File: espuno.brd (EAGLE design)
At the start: 68.6 x 53.3 mm, 62 parts, among them J1 ARDUINO_R3_SHIELD, T1 FDN340P, U1 ADS1115IDGST, U2 NCP1117ST50T3G, U3 LP2985-33DBVR, U4 FT232R, U5 LMV358IDGKR, U6 MCP73831, U7 TPS61200, X1 POWERSUPPLY_DC21MMX

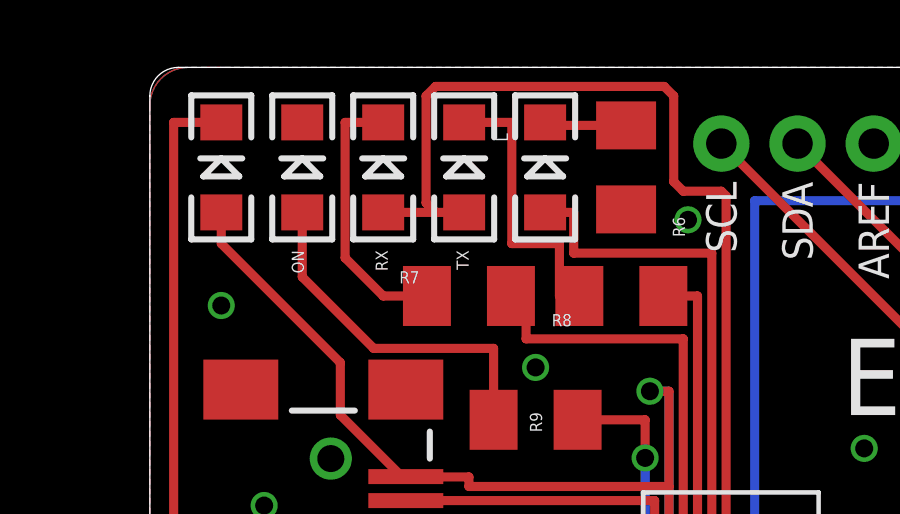
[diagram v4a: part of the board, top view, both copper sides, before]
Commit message: Move some labels, change 'CHARGING' into 'CHRG' for brevity
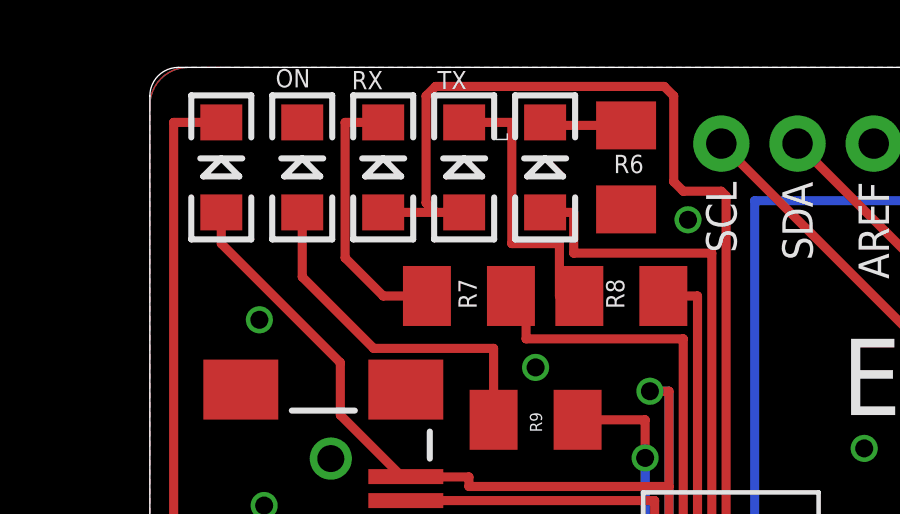
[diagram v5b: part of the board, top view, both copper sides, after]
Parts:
- D4: value CHARGING -> CHRG
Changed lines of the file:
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@@
 </element>
 <element name="ON" library="SparkFun-LED" package="LED-1206" value="GREEN" x="5.08" y="50.00625" smashed="yes" rot="R90">
-<attribute name="NAME" x="4.73075" y="47.244" size="0.4064" layer="25" rot="R270"/>
+<attribute name="NAME" x="4.191" y="52.67325" size="0.6096" layer="25"/>
 </element>
 <element name="D1" library="diode" package="SMB" value="M7" x="18.25625" y="2.38125" smashed="yes" rot="R180">
@@
 </element>
 <element name="R6" library="rcl" package="M1206" value="1K" x="15.875" y="50.00625" smashed="yes" rot="R90">
-<attribute name="NAME" x="17.43075" y="48.35525" size="0.4064" layer="25" font="vector" rot="R270"/>
+<attribute name="NAME" x="15.46225" y="49.81575" size="0.6096" layer="25" font="vector"/>
 </element>
 <element name="R9" library="rcl" package="M1206" value="470" x="12.85875" y="41.5925" smashed="yes" rot="R180">
@@
 </element>
 <element name="R7" library="rcl" package="M1206" value="330" x="10.63625" y="45.72" smashed="yes" rot="R180">
-<attribute name="NAME" x="8.98525" y="46.5455" size="0.4064" layer="25" font="vector" rot="R180"/>
+<attribute name="NAME" x="10.287" y="46.2915" size="0.6096" layer="25" font="vector" rot="R270"/>
 </element>
 <element name="R8" library="rcl" package="M1206" value="330" x="15.71625" y="45.72" smashed="yes" rot="R180">
-<attribute name="NAME" x="14.06525" y="45.11675" size="0.4064" layer="25" font="vector" rot="R180"/>
+<attribute name="NAME" x="15.20825" y="46.2915" size="0.6096" layer="25" font="vector" rot="R270"/>
 </element>
 <element name="RX" library="SparkFun-LED" package="LED-1206" value="GREEN" x="7.77875" y="50.00625" smashed="yes" rot="R90">
-<attribute name="NAME" x="7.52475" y="47.244" size="0.4064" layer="25" rot="R270"/>
+<attribute name="NAME" x="6.731" y="52.60975" size="0.6096" layer="25"/>
 </element>
 <element name="TX" library="SparkFun-LED" package="LED-1206" value="RED" x="10.4775" y="50.00625" smashed="yes" rot="R90">
-<attribute name="NAME" x="10.2235" y="47.244" size="0.4064" layer="25" rot="R270"/>
+<attribute name="NAME" x="9.5885" y="52.60975" size="0.6096" layer="25"/>
 </element>
 <element name="SV1" library="con-lstb" package="MA03-2" value="" x="64.92875" y="27.94" smashed="yes" rot="R90">
@@
 <attribute name="NAME" x="19.4945" y="19.875496875" size="0.6096" layer="25" rot="R90"/>
 </element>
-<element name="D4" library="SparkFun-LED" package="LED-1206" value="CHARGING" x="2.38125" y="50.00625" smashed="yes" rot="R90">
-<attribute name="VALUE" x="2.20533125" y="47.3357875" size="0.4064" layer="27" rot="R270"/>
+<element name="D4" library="SparkFun-LED" package="LED-1206" value="CHRG" x="2.38125" y="50.00625" smashed="yes" rot="R90">
+<attribute name="VALUE" x="0.9242125" y="52.68783125" size="0.6096" layer="27"/>
 </element>
 <element name="R10" library="rcl" package="M1206" value="470" x="4.1275" y="29.68625" smashed="yes" rot="R180">
@@
 <via x="23.8125" y="40.64" extent="1-16" drill="0.6"/>
 <via x="3.81" y="38.735" extent="1-16" drill="0.6"/>
-<via x="2.38125" y="45.4025" extent="1-16" drill="0.6"/>
+<via x="3.65125" y="44.92625" extent="1-16" drill="0.6"/>
 <via x="12.85875" y="43.33875" extent="1-16" drill="0.6"/>
 <via x="22.70125" y="3.175" extent="1-16" drill="0.6"/>
